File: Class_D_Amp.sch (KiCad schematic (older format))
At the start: 65 parts

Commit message: Minor updates
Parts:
- added C13, C14: 100u, e5spk:CP_Elec_12.5x13, symbol CP_Small
- C1, C10, C11, C12, C15, C16, C17, C18, C19, C2, C20, C21, C22, C3, C6, C7, C8, C9: renamed from C?; footprint (none) -> Capacitors_SMD:C_0805
- C4, C5: renamed from C?; footprint (none) -> e5spk:CP_Elec_12.5x13
- CON1: renamed from CON?; footprint (none) -> Connect:BARREL_JACK
- D1, D2, D3, D4, D5, D6: renamed from D?; footprint (none) -> Diodes_SMD:D_0805
- P1, P2: renamed from P?; footprint (none) -> Terminal_Blocks:TerminalBlock_bornier-2_P5.08mm
- Q1, Q2: renamed from Q?; footprint (none) -> TO_SOT_Packages_SMD:SOT-23
- Q3, Q4, Q5, Q6: renamed from Q?; footprint (none) -> TO_SOT_Packages_SMD:TO-252-2
- R1, R10, R11, R12, R13, R14, R15, R16, R17, R18, R19, R2, R20, R21, R22, R3, R4, R5, R6, R7, R8, R9: renamed from R?; footprint (none) -> Resistors_SMD:R_0805
- U1, U2, U3, U4, U5, U6: renamed from U?; footprint (none) -> Housings_SOIC:SOIC-8_3.9x4.9mm_Pitch1.27mm
- gave numbers to parts that had none: 2
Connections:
- net GND: now also C13.2, C14.1
- net VDD: now also C13.1
- net VSS: now also C14.2

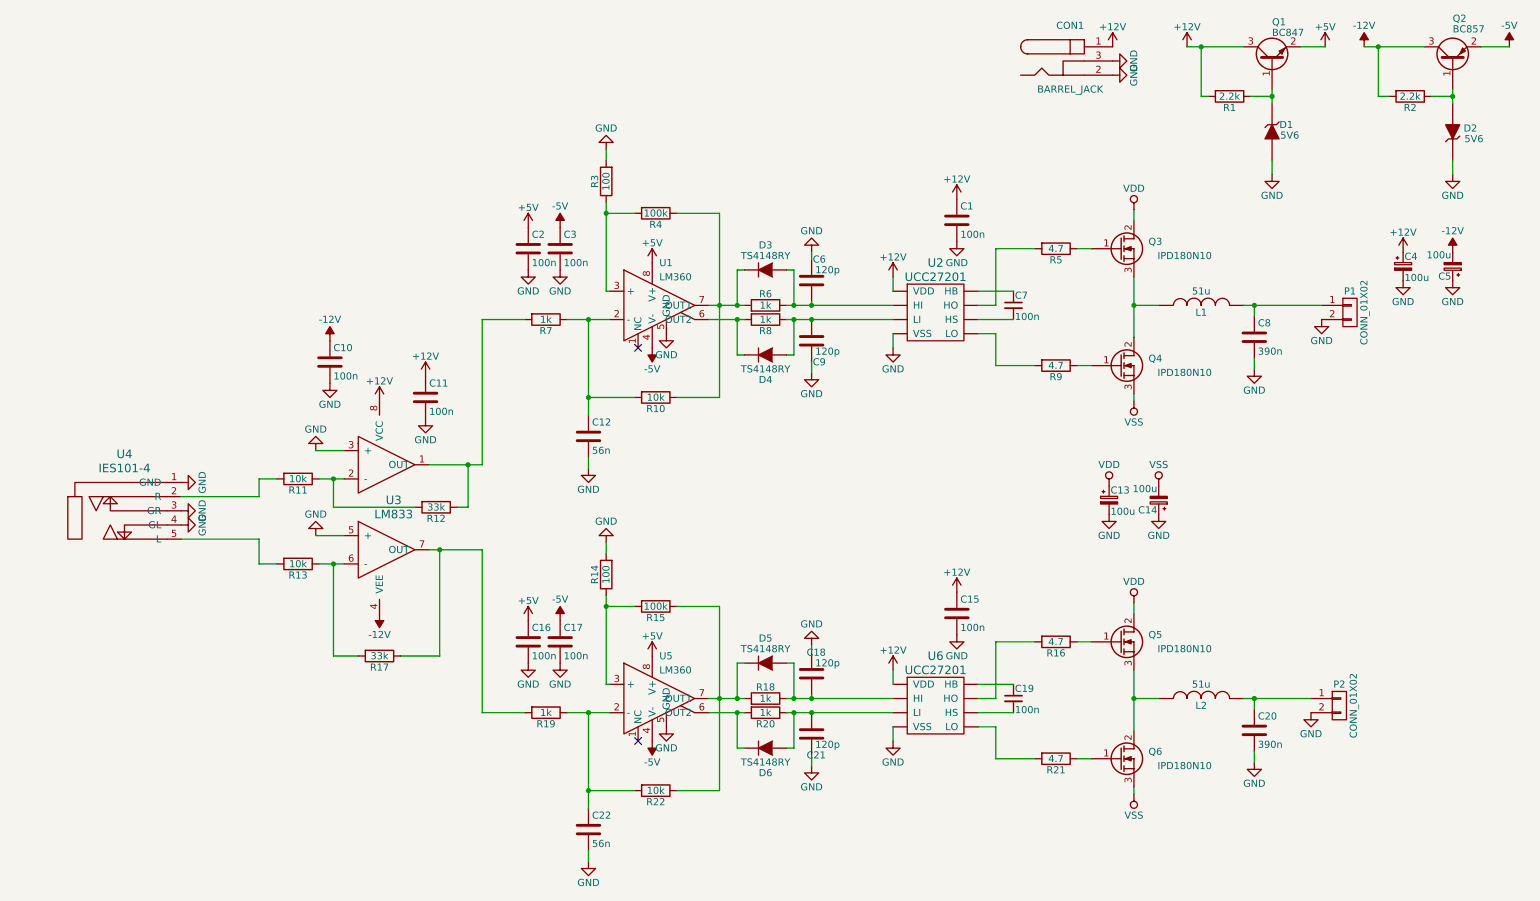
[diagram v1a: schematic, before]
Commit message: Fixed Issues in Schematic + Generated netlist
Changed feedback to come from output nodes.
Fixed Driver supplies
Added global decoupling
Hopefully fixed supply pumping
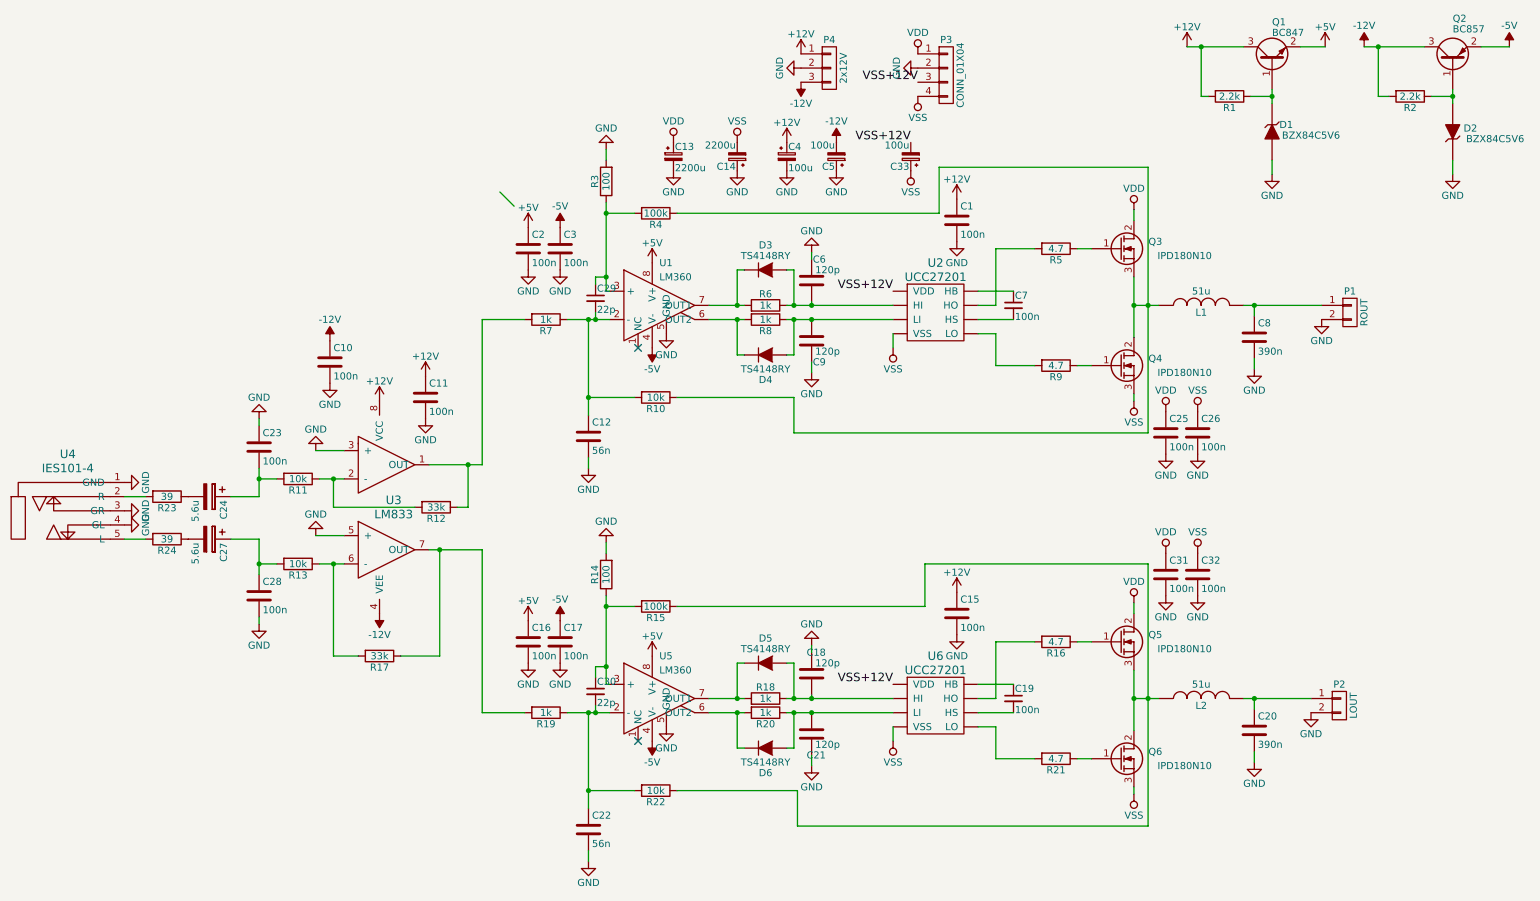
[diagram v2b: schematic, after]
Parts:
- removed CON1: BARREL_JACK, Connect:BARREL_JACK, symbol BARREL_JACK
- added C23, C25, C26, C28, C31, C32: 100n, Capacitors_SMD:C_0805, symbol C
- added C24, C27: 5.6u, Capacitors_ThroughHole:CP_Radial_D5.0mm_P2.00mm, symbol CP
- added C29, C30: 22p, Capacitors_SMD:C_0805, symbol C_Small
- added C33: 100u, Capacitors_ThroughHole:CP_Radial_D6.3mm_P2.50mm, symbol CP_Small
- added P3: CONN_01X04, Terminal_Blocks:TerminalBlock_bornier-4_P5.08mm, symbol CONN_01X04
- added P4: 2x12V, Terminal_Blocks:TerminalBlock_bornier-3_P5.08mm, symbol CONN_01X03
- added R23, R24: 39, Resistors_SMD:R_0805, symbol R
- C13, C14: value 100u -> 2200u; footprint e5spk:CP_Elec_12.5x13 -> Capacitors_ThroughHole:CP_Radial_D16.0mm_P7.50mm
- C20, C8: footprint Capacitors_SMD:C_0805 -> Capacitors_ThroughHole:C_Rect_L7.0mm_W3.5mm_P5.00mm
- C4, C5: footprint e5spk:CP_Elec_12.5x13 -> Capacitors_ThroughHole:CP_Radial_D6.3mm_P2.50mm
- D1, D2: value 5V6 -> BZX84C5V6; footprint Diodes_SMD:D_0805 -> TO_SOT_Packages_SMD:SOT-23
- L1, L2: footprint (none) -> e5spk:3C20
- P1: value CONN_01X02 -> ROUT
- P2: value CONN_01X02 -> LOUT
- R16, R21, R5, R9: footprint Resistors_SMD:R_0805 -> Resistors_SMD:R_1206
- U4: footprint Housings_SOIC:SOIC-8_3.9x4.9mm_Pitch1.27mm -> Connect:Stereo_Jack_3.5mm_Switch_Ledino_KB3SPRS
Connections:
- net +12V: now also P4.1 (P1); no longer U2.~ (VSS), U6.~ (VSS)
- net -12V: now also P4.3 (P3)
- net GND: now also C23.1, C25.2, C26.2, C28.2, C31.2, C32.2, P3.2 (P2), P4.2 (P2); no longer U2.~ (VSS), U6.~ (VSS)
- net VDD: now also C25.1, C31.1, P3.1 (P1)
- net VSS: now also U2.~ (VSS), U6.~ (VSS), C26.1, C32.1, C33.1, P3.4 (P4)
- net at L1.1, Q3.3 (S), Q4.2 (D): now also R10.1, R4.1
- net at C12.1, R10.2, R7.1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: now also C29.2
- net at R3.1, R4.2, U1.3 (+): now also C29.1
- net at D3.1 (K), R6.2, U1.7 (OUT1): no longer R10.1, R4.1
- net at L2.1, Q5.3 (S), Q6.2 (D): now also R15.1, R22.1
- net at C22.1, R19.1, R22.2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: now also C30.2
- net at R14.1, R15.2, U5.3 (+): now also C30.1
- net at D5.1 (K), R18.2, U5.7 (OUT1): no longer R15.1, R22.1
- net at R13.2: now also C27.1, C28.1; no longer U4.5 (L)
- net at R11.2: now also C23.2, C24.1; no longer U4.2 (R)
- new net: R23.2, U4.2 (R)
- new net: R24.2, U4.5 (L)
- new net: C24.2, R23.1
- new net: C27.2, R24.1
- new net VSS+12V: C33.2, P3.3 (P3), U2.~ (VSS), U6.~ (VSS)
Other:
- moved on the sheet: C13, C14, C4, C5, U4
